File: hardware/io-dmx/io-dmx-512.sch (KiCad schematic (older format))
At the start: 26 parts, among them J1 IO EXTENSION, J2 NC3FAH/NC5FAH, J3 NC3MAH/NC5MAH, U1 NMA0505SC, U2 6N137, U3 6N137, U4 6N137, U5 MAX3485CPA+

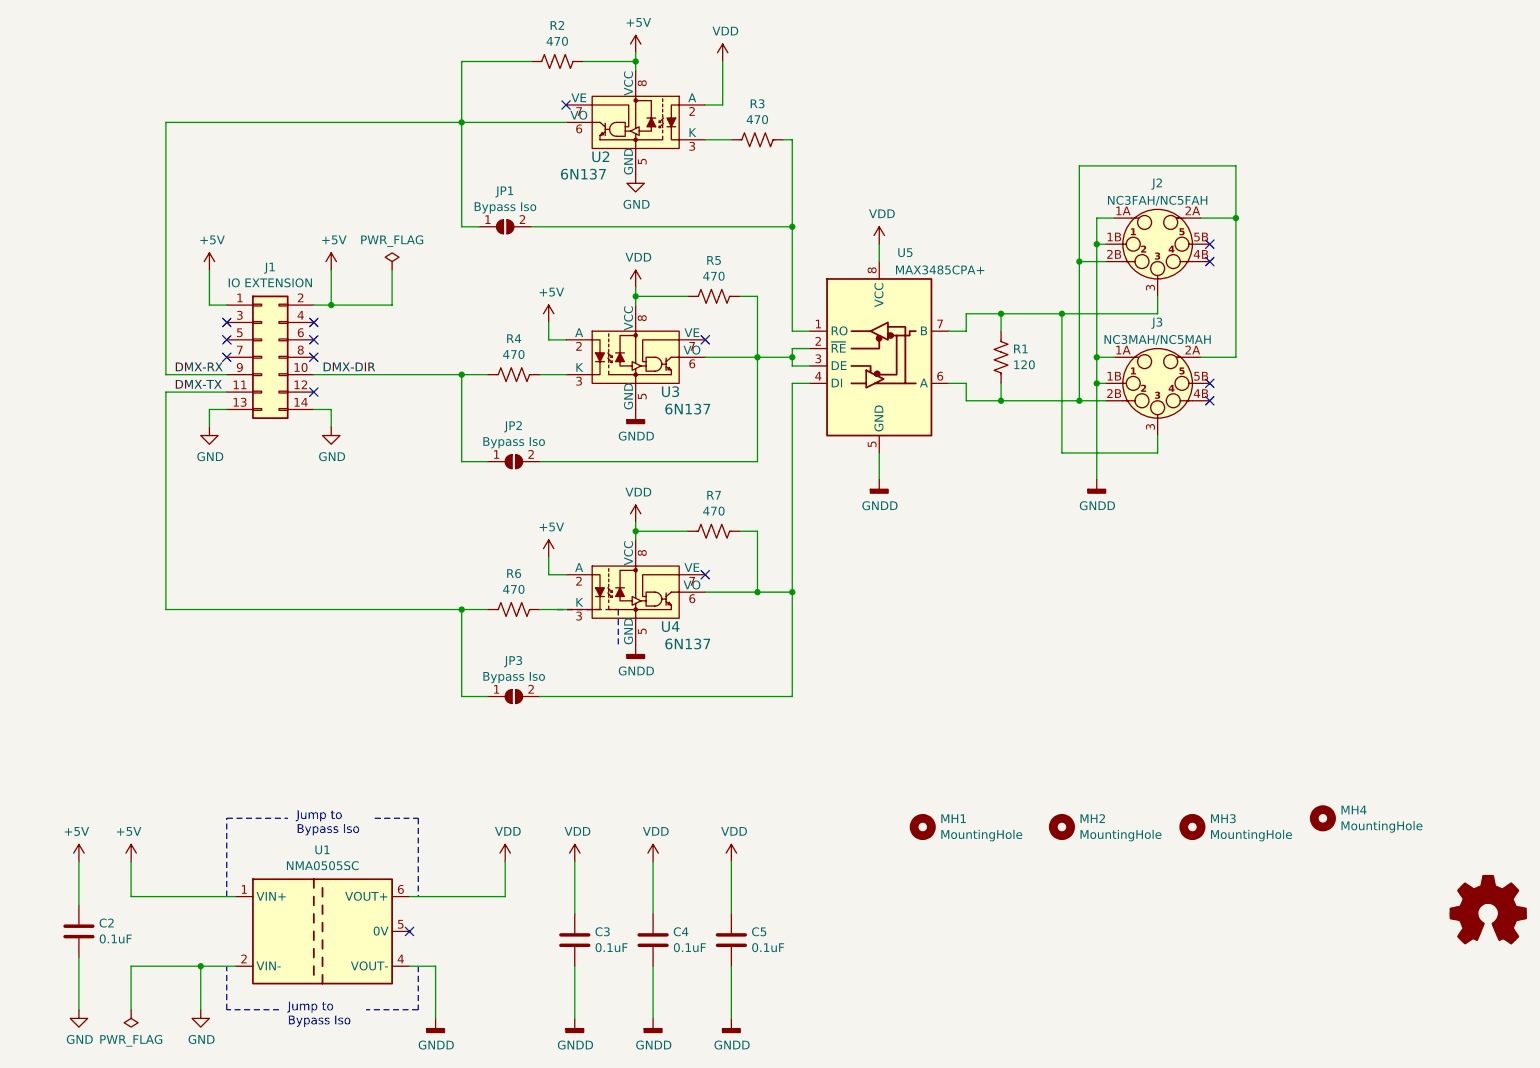
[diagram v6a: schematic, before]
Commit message: - Added termination switch - Change to RFM-0505S - Change to MAX485E - Swap A and B on Max485 - Avoid split power planes under WH4 - Remove pads from XLR alignment pins - Update readme - Add IO1 parts to BOM generation.
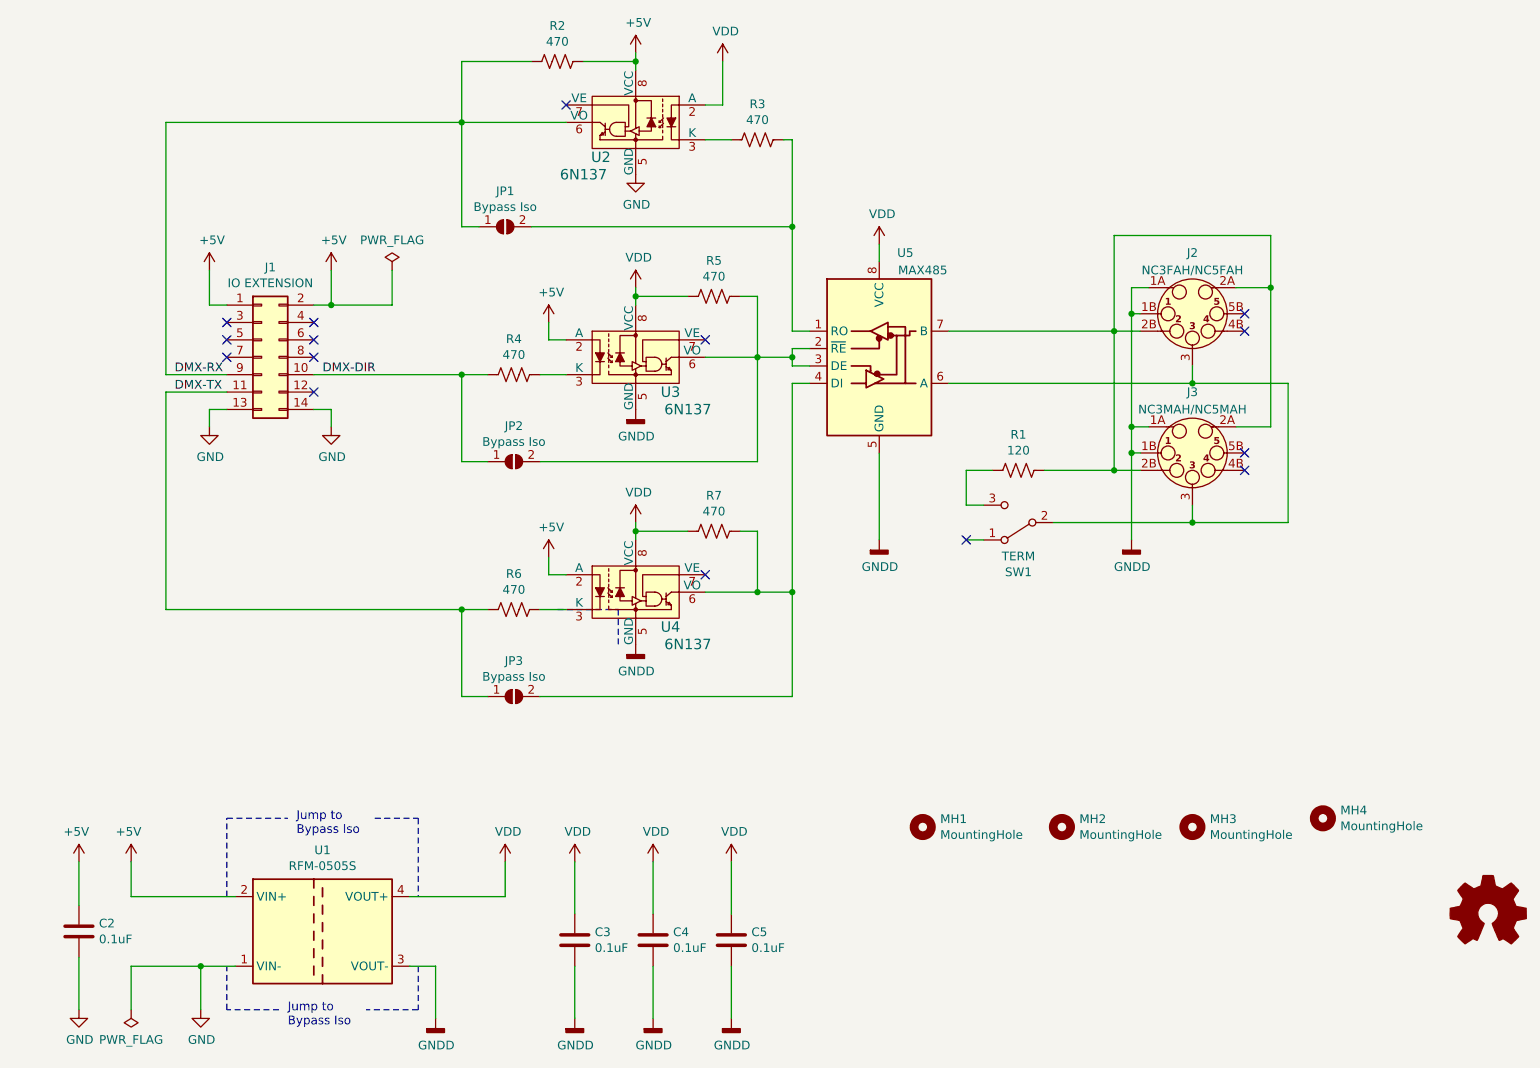
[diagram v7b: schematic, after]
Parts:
- removed U1: NMA0505SC, footprints:Converter_DCDC_muRata_NMAxxxxSC_THT_Bypass, symbol Regulator_Switching:NMA0505SC
- added SW1: TERM, footprints:ESWITCH_1218_SPDT, symbol Switch:SW_SPDT
- added U1: RFM-0505S, footprints:Converter_DCDC_Recom_RFM0505S_THT_Bypass, symbol DMXDemonstrator:RFM-0505S
- C2, C3, C4, C5: AF_Detail_Page https://www.adafruit.com/product/753 -> (none); AF_PN 753 -> (none); MO_Detail_Page https://www.mouser.com/ProductDetail/KEMET/C320C104K5R5TA73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 -> (none); MO_PN 80-C320C104K5R7301 -> (none); NW_Detail_Page https://www.newark.com/kemet/c315c104m5u5ta/capacitor-mlcc-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 -> (none); NW_PN 13K6284 -> (none); PartId (none) -> C_DECOUPLE; SP_Detail_Page https://www.sparkfun.com/products/8375 -> (none); SP_PN COM-08375 -> (none)
- J1: MO_Detail_Page https://www.mouser.com/ProductDetail/Wurth-Elektronik/61201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 -> (none); MO_PN 710-61201421721 -> (none); NW_Detail_Page https://www.newark.com/wurth-elektronik/612014235221/conn-r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 -> (none); NW_PN 75AJ1395 -> (none); PartId (none) -> H_IO_RA,JP_IO
- J2: MO_Detail_Page https://www.mouser.com/ProductDetail/Neutrik/NC5FAH/?qs=JfN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 -> (none); MO_PN 568-NC5FAH -> (none); NW_Detail_Page https://www.newark.com/neutrik/nc5fah/connector-xlr-recepta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 -> (none); NW_PN 94C1524 -> (none); PartId (none) -> J_XLR5F
- J3: MO 568-NC5MAH -> (none); MO_Detail_page https://www.mouser.com/ProductDetail/Neutrik/NC5MAH/?qs=43p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 -> (none); NW_Detail_Page https://www.newark.com/neutrik/nc5mah/connector-xlr-audio-p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 -> (none); NW_PM 25C4313 -> (none); PartId (none) -> J_XLR5M
- JP1, JP2, JP3: PartId (none) -> JP_SOLDER
- R1: Description DMX Termination -> (none); MO_Detail_Page https://www.mouser.com/ProductDetail/Yageo/CFR-25JT-52-120R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 -> (none); MO_PN 603-CFR-25JT-52-120R -> (none); NW_Detail_Page https://www.newark.com/multicomp-pro/mcf-0-25w-120r/carbon-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 -> (none); NW_PN 38K0333 -> (none); PartId (none) -> R_120
- R2, R3, R4, R5, R6, R7: AF_Detail_Page https://www.adafruit.com/product/2781 -> (none); AF_PN 2781 -> (none); MO_Detail_Page https://www.mouser.com/ProductDetail/Yageo/CFR-25JT-52-470R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 -> (none); MO_PN 603-CFR-25JT-52-470R -> (none); NW_Detail_Page https://www.newark.com/multicomp-pro/mcf-0-25w-470r/carbon-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 -> (none); NW_PN 38K0375 -> (none); PartId (none) -> R_470
- U2: DK_Datasheet_Link https://media.digikey.com/pdf/Data%20Sheets/Lite-On%20PDFs/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 -> (none); DK_Detail_Page /product-detail/en/lite-on-inc/6N137/160-1791-ND/1969175 -> (none); MO_Detail_Page https://www.mouser.com/ProductDetail/Vishay-Semiconductors/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 -> (none); MO_PN 782-6N137 -> (none); NW_Detail_Page https://www.newark.com/vishay/6n137/optocoupler-transistor-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 -> (none); NW_PN 52M1895 -> (none); PartId (none) -> U_6N137; Status Active -> (none)
- U3, U4: DK_Datasheet_Link https://media.digikey.com/pdf/Data%20Sheets/Lite-On%20PDFs/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 -> (none); DK_Detail_Page /product-detail/en/lite-on-inc/6N137/160-1791-ND/1969175 -> (none); MO_Detail_Page https://www.mouser.com/ProductDetail/Vishay-Semiconductors/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 -> (none); MO_PN 782-6N137 -> (none); NW_Detail_Page https://www.newark.com/vishay/6n137/optocoupler-transistor-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 -> (none); NW_PN 52M1895 -> (none); PartId (none) -> U_6N137
- U5: value MAX3485CPA+ -> MAX485; DK_Page_Detail products/detail/MAX3485CPA%2B/MAX3485CPA%2B-ND/1702227 -> (none); Digi-Key_PN MAX3485CPA+-ND -> (none); MO_Detail_Page https://www.mouser.com/ProductDetail/Maxim-Integrated/MAX34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 -> (none); MO_PN 700-MAX3485CPA -> (none); NW_Detail_Page https://www.newark.com/maxim-integrated-products/max3485cpa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 -> (none); NW_PN 81Y9431 -> (none); PartId (none) -> U_485
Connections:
- net +5V: now also U1.2 (VIN+)
- net GND: now also U1.1 (VIN-)
- net GNDD: now also U1.3 (VOUT-)
- net VDD: now also U1.4 (VOUT+)
- net at J2.2A (7), J2.2B (P2), J3.2A (7)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: now also U5.7 (B); no longer U5.6 (A)
- net at J2.3 (P3), J3.3 (P3): now also U5.6 (A), SW1.2 (B); no longer R1.2, U5.7 (B)
- new net: R1.2, SW1.3 (C)
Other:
- moved on the sheet: J2, J3
